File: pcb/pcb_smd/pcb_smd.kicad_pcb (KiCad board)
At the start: 2 copper layers, 53.3 x 47 mm, 50 parts, among them J1 USB_B_Micro, J2 AVR-ISP-6, J3 Conn_01x02, SW1 SW_Push, SW2 SW_Push, SW3 SW_Push, U1 ATmega32U4-MU, U2 LTC-4627, U3 MPXV5010, U4 MPXV5010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

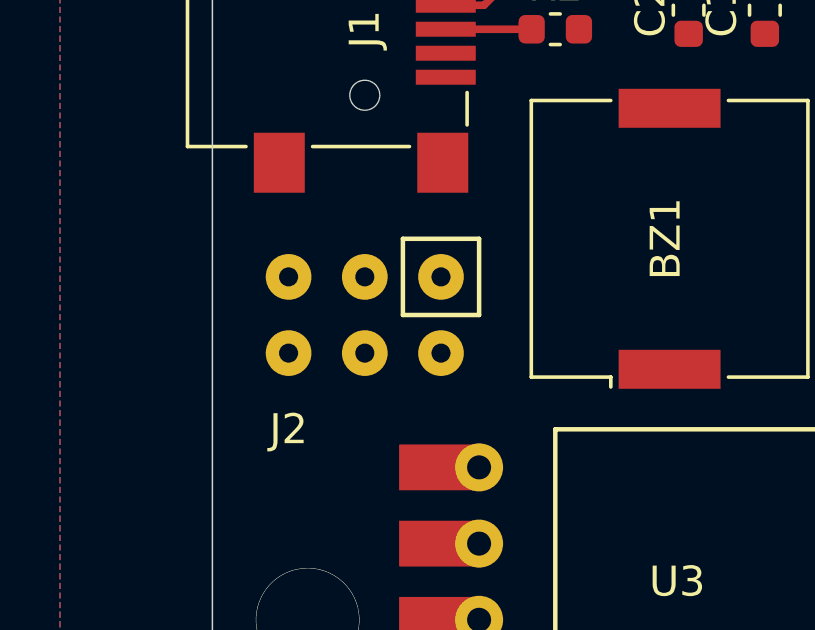
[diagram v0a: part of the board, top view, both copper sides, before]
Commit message: switch pogo size
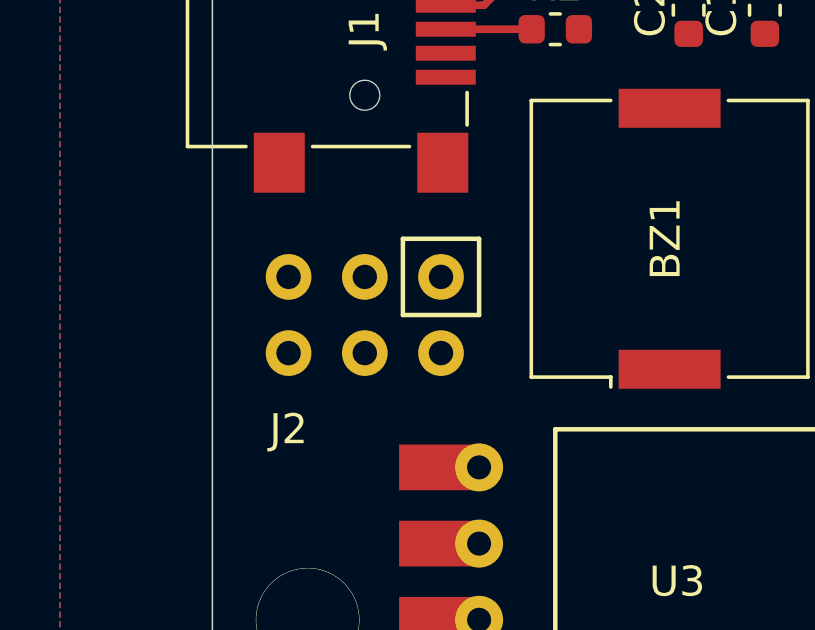
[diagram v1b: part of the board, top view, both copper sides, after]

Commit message: finish smd version
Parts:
- removed C10, C11, C12: C, Capacitor_SMD:C_0603_1608Metric
- removed R17: 470, Resistor_SMD:R_0603_1608Metric
- removed U4: MPXV5010, common:DIPSOP-8_W550thou
- added G***: LOGO, LOGO, B.Cu at (162.6, 66.0)
- C1, C13, C2, C4, C6, C8, C9: value C -> 1uF
- C3: value C -> 0.1uF
- C5: value C -> .01uF
- J2: moved to B.Cu
- L1: value L -> 47nH
- R1: value R -> 10k
- R4: value R -> 2
- U1: footprint common:QFN-44 -> Package_QFP:TQFP-44_10x10mm_P0.8mm
- moved R5 46.6 mm to (123.2, 78.7), turned to 0 degrees
- moved C9 44.4 mm to (123.2, 76.2), turned to 0 degrees
- moved D5 42.4 mm to (123.2, 73.7), turned to 0 degrees
- moved J1 40.9 mm to (160.7, 99.7), turned to 0 degrees
- moved R7 37.8 mm to (123.2, 94.0), turned to 0 degrees
- moved SW2 37.5 mm to (128.9, 88.3), turned to -90 degrees
- moved SW1 37.5 mm to (128.9, 77.5), turned to -90 degrees
- moved R6 36.2 mm to (123.2, 86.4), turned to 0 degrees
- moved C7 34.7 mm to (123.2, 91.4), turned to 0 degrees
- moved D1 34.4 mm to (151.8, 102.9), turned to 0 degrees
- moved C8 33.8 mm to (123.2, 83.8), turned to 0 degrees
- moved D3 31.6 mm to (123.2, 88.9), turned to 0 degrees
- moved D4 31.6 mm to (123.2, 81.3), turned to 0 degrees
- moved R4 29.2 mm to (151.8, 100.3), turned to 0 degrees
- moved BZ1 26.8 mm to (161.3, 90.2), turned to 0 degrees
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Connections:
- C13 pad 1: /VREF -> /AREF
- R10 pad 1: (no net) -> /c
- R11 pad 1: (no net) -> /d
- R12 pad 1: (no net) -> /e
- R13 pad 1: (no net) -> /f
- R14 pad 1: (no net) -> /g
- R15 pad 1: (no net) -> /DP
- R20 pad 2: /VREF -> /AREF
- R8 pad 1: (no net) -> /a
- R9 pad 1: (no net) -> /b
- U1 pad 18: (no net) -> /DIG2
- U1 pad 19: (no net) -> /DIG:
- U1 pad 20: (no net) -> /DIG3
- U1 pad 21: (no net) -> /DIG4
- U1 pad 25: /PRESSURE2 -> /DP
- U1 pad 26: /PRESSURE1 -> /f
- U1 pad 27: (no net) -> /e
- U1 pad 28: (no net) -> /c
- U1 pad 29: (no net) -> /d
- U1 pad 30: (no net) -> /g
- U1 pad 31: (no net) -> /a
- U1 pad 32: (no net) -> /b
- U1 pad 33: (no net) -> /DIG1
- U1 pad 41: (no net) -> /PRESSURE1
- U1 pad 42: (no net) -> /AREF
- U2 pad 1: (no net) -> /DIG1
- U2 pad 2: (no net) -> /DIG2
- U2 pad 4: (no net) -> /DIG:
- U2 pad 6: (no net) -> /DIG3
- U2 pad 8: (no net) -> /DIG4
- U5 pad 1: /VREF -> /AREF
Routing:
- net +5V: track 12.4 -> 83.2 mm, vias 0 -> 4
- net Net-(C3-Pad1): track 0.00 -> 29.8 mm, vias 0 -> 2
- net Net-(R7-Pad2): track 0.00 -> 23.5 mm
- net /DIG2: track 0.00 -> 17.5 mm, vias 0 -> 1
- net /b: track 0.00 -> 16.5 mm
- net /a: track 0.00 -> 15.9 mm
- net /RST: track 0.00 -> 15.5 mm, vias 0 -> 1
- net Net-(R6-Pad2): track 0.00 -> 15.1 mm
- net Net-(R5-Pad2): track 0.00 -> 15.1 mm
- net GND: track 0.00 -> 13.9 mm, vias 4 -> 11
- net Net-(J1-Pad2): track 3.67 -> 17.4 mm
- net /DIG:: track 0.00 -> 13.2 mm, vias 0 -> 1
- net Net-(J1-Pad3): track 2.86 -> 16.0 mm
- net /d: track 0.00 -> 13.0 mm
- net /g: track 0.00 -> 12.6 mm
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- added copper zone on B.Cu, net GND
- removed copper zone on B.Cu, net (none)
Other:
- board text added: "Evan Widloski 2020-06-19 RapidAlarm v2"

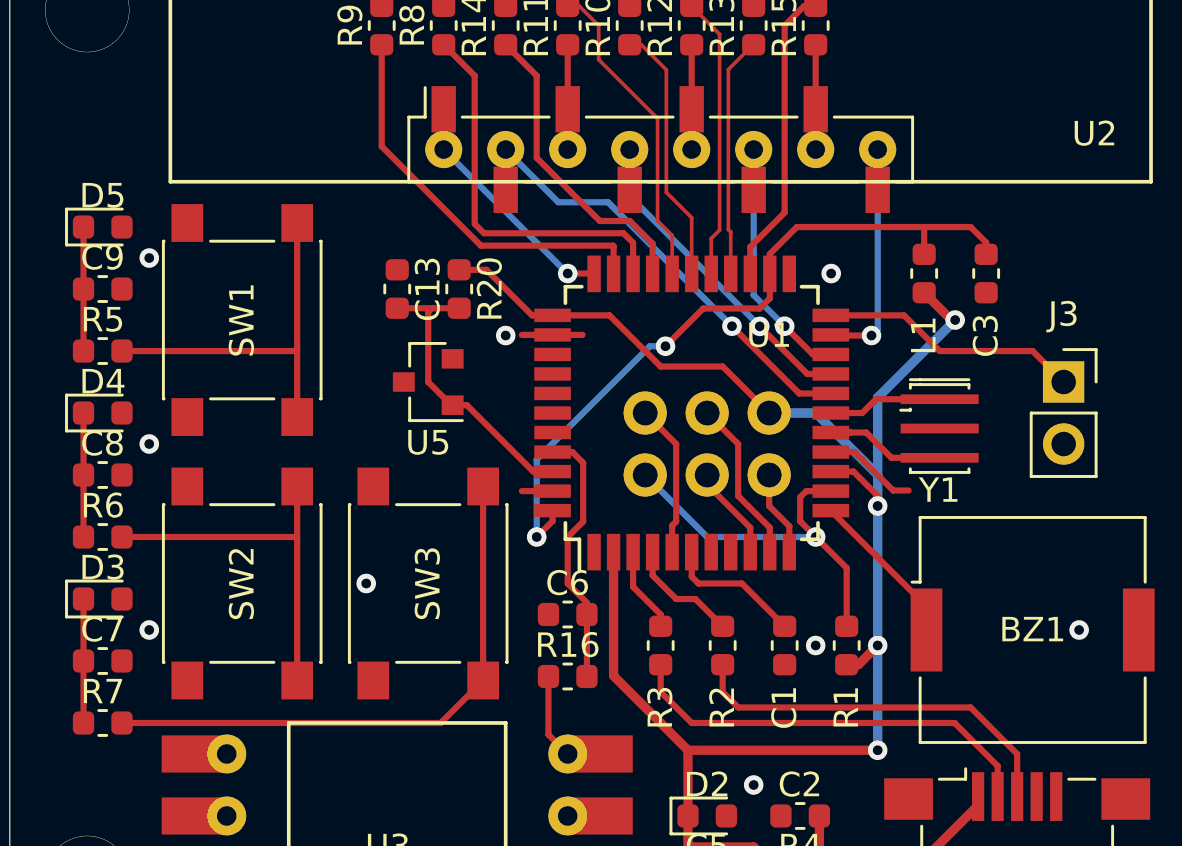
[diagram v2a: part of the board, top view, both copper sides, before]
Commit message: fix TX pin, fix VBUS
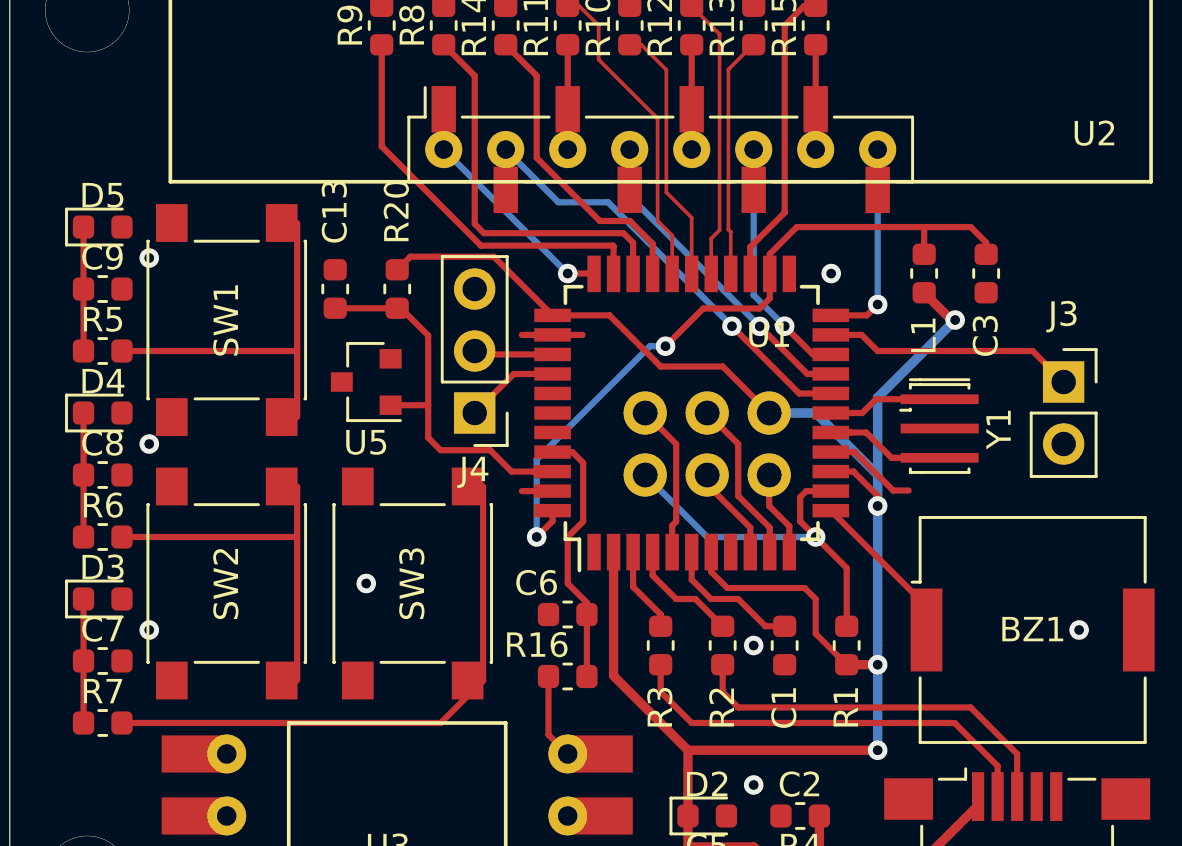
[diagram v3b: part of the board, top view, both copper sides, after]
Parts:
- removed G***: LOGO, LOGO
- added J4: Conn_01x03, Connector_PinHeader_2.54mm:PinHeader_1x03_P2.54mm_Vertical, F.Cu at (138.4, 81.3)
- R2, R3: value R -> 22
- Y1: value Crystal_GND2_Small -> Resonator
- moved C13 2.54 mm to (132.7, 76.2)
- moved R20 2.54 mm to (135.3, 76.2)
- moved U5 2.54 mm to (134.0, 80.0)
- moved SW3 0.64 mm to (135.9, 88.3)
- moved SW1 0.63 mm to (128.3, 77.5)
- moved SW2 0.63 mm to (128.3, 88.3)
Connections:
- U1 pad 21: /DIG4 -> Net-(J3-Pad1)
- U1 pad 22: Net-(J3-Pad1) -> /DIG4
- U1 pad 36: (no net) -> Net-(J4-Pad2)
- U1 pad 37: (no net) -> Net-(J4-Pad1)
- U1 pad 7: (no net) -> +5V
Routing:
- net +5V: track 83.2 -> 94.6 mm
- net /AREF: track 12.2 -> 16.5 mm
- net Net-(J4-Pad1): track 0.00 -> 3.85 mm
- net Net-(J4-Pad2): track 0.00 -> 3.25 mm
- net /DIG4: track 9.40 -> 8.45 mm
- net GND: vias 11 -> 10
